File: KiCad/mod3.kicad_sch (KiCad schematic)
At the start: 49 parts, among them M5 Fan_4pin, M6 Fan_4pin, U3 ZD25Q64BSIGT

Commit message: Add most passive component footprints
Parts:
- C57, C58, C59, C60, C61, C62, C63, C64, C65, C66, C67, C68, C69, C70, C71, C72, C73, C74, C75, C76, C77, C78, C79: footprint Capacitor_SMD:C_0603_1608Metric -> Capacitor_SMD:C_0402_1005Metric
- D10, D9: footprint (none) -> LED_SMD:LED_0603_1608Metric
- D11, D12: footprint (none) -> Diode_SMD:D_SOD-123
- M5, M6: footprint (none) -> Connector:FanPinHeader_1x04_P2.54mm_Vertical
- R45, R57: value 510R -> 2.2k; footprint (none) -> Resistor_SMD:R_0402_1005Metric
- R46, R47, R48, R50, R51, R52, R53, R54, R56, R58, R61, R62: footprint (none) -> Resistor_SMD:R_0402_1005Metric
- R49: footprint (none) -> Resistor_SMD:R_0805_2012Metric
- R55, R59, R60: value 21.5k -> 22k; footprint (none) -> Resistor_SMD:R_0402_1005Metric
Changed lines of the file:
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@@
 			)
 		)
-		(property "Footprint" ""
+		(property "Footprint" "Resistor_SMD:R_0402_1005Metric"
 			(at 323.85 54.61 0)
 			(effects
@@
 			)
 		)
-		(property "Footprint" "Capacitor_SMD:C_0603_1608Metric"
+		(property "Footprint" "Capacitor_SMD:C_0402_1005Metric"
 			(at 223.52 168.91 0)
 			(effects
@@
 			)
 		)
-		(property "Footprint" "Capacitor_SMD:C_0603_1608Metric"
+		(property "Footprint" "Capacitor_SMD:C_0402_1005Metric"
 			(at 223.52 158.75 0)
 			(effects
@@
 			)
 		)
-		(property "Footprint" ""
+		(property "Footprint" "LED_SMD:LED_0603_1608Metric"
 			(at 320.04 153.67 0)
 			(effects
@@
 			)
 		)
-		(property "Footprint" ""
+		(property "Footprint" "Resistor_SMD:R_0402_1005Metric"
 			(at 320.04 128.27 0)
 			(effects
@@
 			)
 		)
-		(property "Value" "21.5k"
+		(property "Value" "22k"
 			(at 380.492 51.562 90)
 			(effects
@@
 			)
 		)
-		(property "Footprint" ""
+		(property "Footprint" "Resistor_SMD:R_0402_1005Metric"
 			(at 378.46 49.53 0)
 			(effects
@@
 			)
 		)
-		(property "Footprint" ""
+		(property "Footprint" "Connector:FanPinHeader_1x04_P2.54mm_Vertical"
 			(at 403.86 51.816 0)
 			(effects
@@
 			)
 		)
-		(property "Footprint" "Capacitor_SMD:C_0603_1608Metric"
+		(property "Footprint" "Capacitor_SMD:C_0402_1005Metric"
 			(at 223.52 163.83 0)
 			(effects
@@
 			)
 		)
-		(property "Footprint" ""
+		(property "Footprint" "Resistor_SMD:R_0402_1005Metric"
 			(at 321.31 250.19 0)
 			(effects
@@
 			)
 		)
-		(property "Footprint" ""
+		(property "Footprint" "Diode_SMD:D_SOD-123"
 			(at 382.27 44.45 0)
 			(effects
@@
 			)
 		)
-		(property "Footprint" "Capacitor_SMD:C_0603_1608Metric"
+		(property "Footprint" "Capacitor_SMD:C_0402_1005Metric"
 			(at 223.52 173.99 0)
 			(effects
@@
 			)
 		)
-		(property "Footprint" "Capacitor_SMD:C_0603_1608Metric"
+		(property "Footprint" "Capacitor_SMD:C_0402_1005Metric"
 			(at 320.04 44.45 0)
 			(effects
@@
 			)
 		)
-		(property "Value" "21.5k"
+		(property "Value" "22k"
 			(at 325.882 51.562 90)
 			(effects
@@
 			)
 		)
-		(property "Footprint" ""
+		(property "Footprint" "Resistor_SMD:R_0402_1005Metric"
 			(at 323.85 49.53 0)
 			(effects
@@
 			)
 		)
-		(property "Footprint" ""
+		(property "Footprint" "Resistor_SMD:R_0402_1005Metric"
 			(at 223.52 224.79 0)
 			(effects
@@
 			)
 		)
-		(property "Footprint" ""
+		(property "Footprint" "Resistor_SMD:R_0402_1005Metric"
 			(at 378.46 54.61 0)
 			(effects
@@
 			)
 		)
-		(property "Footprint" "Capacitor_SMD:C_0603_1608Metric"
+		(property "Footprint" "Capacitor_SMD:C_0402_1005Metric"
 			(at 223.52 140.97 0)
 			(effects
@@
 			)
 		)
-		(property "Footprint" "Capacitor_SMD:C_0603_1608Metric"
+		(property "Footprint" "Capacitor_SMD:C_0402_1005Metric"
 			(at 223.52 138.43 0)
 			(effects
@@
 			)
 		)
-		(property "Footprint" "Capacitor_SMD:C_0603_1608Metric"
+		(property "Footprint" "Capacitor_SMD:C_0402_1005Metric"
 			(at 223.52 115.57 0)
 			(effects
@@
 			)
 		)
-		(property "Footprint" "Capacitor_SMD:C_0603_1608Metric"
+		(property "Footprint" "Capacitor_SMD:C_0402_1005Metric"
 			(at 223.52 118.11 0)
 			(effects
@@
 			)
 		)
-		(property "Footprint" "Capacitor_SMD:C_0603_1608Metric"
+		(property "Footprint" "Capacitor_SMD:C_0402_1005Metric"
 			(at 223.52 107.95 0)
 			(effects
@@
 			)
 		)
-		(property "Footprint" "Capacitor_SMD:C_0603_1608Metric"
+		(property "Footprint" "Capacitor_SMD:C_0402_1005Metric"
 			(at 370.84 44.45 0)
 			(effects
@@
 			)
 		)
-		(property "Footprint" "Capacitor_SMD:C_0603_1608Metric"
+		(property "Footprint" "Capacitor_SMD:C_0402_1005Metric"
 			(at 223.52 95.25 0)
 			(effects
@@
 			)
 		)
-		(property "Footprint" ""
+		(property "Footprint" "Resistor_SMD:R_0402_1005Metric"
 			(at 223.52 300.99 0)
 			(effects
@@
 			)
 		)
-		(property "Footprint" "Capacitor_SMD:C_0603_1608Metric"
+		(property "Footprint" "Capacitor_SMD:C_0402_1005Metric"
 			(at 223.52 151.13 0)
 			(effects
@@
 			)
 		)
-		(property "Footprint" ""
+		(property "Footprint" "Resistor_SMD:R_0402_1005Metric"
 			(at 392.43 44.45 0)
 			(effects
@@
 			)
 		)
-		(property "Footprint" "Capacitor_SMD:C_0603_1608Metric"
+		(property "Footprint" "Capacitor_SMD:C_0402_1005Metric"
 			(at 223.52 171.45 0)
 			(effects
@@
 			)
 		)
-		(property "Footprint" "Capacitor_SMD:C_0603_1608Metric"
+		(property "Footprint" "Capacitor_SMD:C_0402_1005Metric"
 			(at 223.52 184.15 0)
 			(effects
@@
 			)
 		)
-		(property "Footprint" ""
+		(property "Footprint" "Resistor_SMD:R_0402_1005Metric"
 			(at 223.52 262.89 0)
 			(effects
@@
 			)
 		)
-		(property "Footprint" ""
+		(property "Footprint" "Diode_SMD:D_SOD-123"
 			(at 327.66 44.45 0)
 			(effects
@@
 			)
 		)
-		(property "Footprint" ""
+		(property "Footprint" "Resistor_SMD:R_0402_1005Metric"
 			(at 316.23 250.19 0)
 			(effects
@@
 			)
 		)
-		(property "Footprint" "Capacitor_SMD:C_0603_1608Metric"
+		(property "Footprint" "Capacitor_SMD:C_0402_1005Metric"
 			(at 223.52 161.29 0)
 			(effects
@@
 			)
 		)
-		(property "Footprint" "Capacitor_SMD:C_0603_1608Metric"
+		(property "Footprint" "Capacitor_SMD:C_0402_1005Metric"
 			(at 223.52 166.37 0)
 			(effects
@@
 			)
 		)
-		(property "Footprint" ""
+		(property "Footprint" "Resistor_SMD:R_0805_2012Metric"
 			(at 275.59 66.04 0)
 			(effects
@@
 			)
 		)
-		(property "Footprint" ""
+		(property "Footprint" "Connector:FanPinHeader_1x04_P2.54mm_Vertical"
 			(at 349.25 51.816 0)
 			(effects
@@
 			)
 		)
-		(property "Footprint" "Capacitor_SMD:C_0603_1608Metric"
+		(property "Footprint" "Capacitor_SMD:C_0402_1005Metric"
 			(at 223.52 105.41 0)
 			(effects
@@
 			)
 		)
-		(property "Footprint" "Capacitor_SMD:C_0603_1608Metric"
+		(property "Footprint" "Capacitor_SMD:C_0402_1005Metric"
 			(at 223.52 148.59 0)
 			(effects
@@
 			)
 		)
-		(property "Footprint" ""
+		(property "Footprint" "LED_SMD:LED_0603_1608Metric"
 			(at 209.55 77.47 0)
 			(effects
@@
 			)
 		)
-		(property "Footprint" ""
+		(property "Footprint" "Resistor_SMD:R_0402_1005Metric"
 			(at 316.23 276.86 0)
 			(effects
@@
 			)
 		)
-		(property "Footprint" "Capacitor_SMD:C_0603_1608Metric"
+		(property "Footprint" "Capacitor_SMD:C_0402_1005Metric"
 			(at 339.09 246.38 0)
 			(effects
@@
 			)
 		)
-		(property "Footprint" "Capacitor_SMD:C_0603_1608Metric"
+		(property "Footprint" "Capacitor_SMD:C_0402_1005Metric"
 			(at 223.52 176.53 0)
 			(effects
@@
 			)
 		)
-		(property "Footprint" ""
+		(property "Footprint" "Resistor_SMD:R_0402_1005Metric"
 			(at 337.82 44.45 0)
 			(effects
@@
 			)
 		)
-		(property "Footprint" ""
+		(property "Footprint" "Resistor_SMD:R_0402_1005Metric"
 			(at 320.04 125.73 0)
 			(effects
@@
 			)
 		)
-		(property "Value" "510R"
+		(property "Value" "2.2k"
 			(at 212.09 71.1199 0)
 			(effects
@@
 			)
 		)
-		(property "Footprint" ""
+		(property "Footprint" "Resistor_SMD:R_0402_1005Metric"
 			(at 209.55 69.85 0)
 			(effects
@@
 			)
 		)
-		(property "Value" "510R"
+		(property "Value" "2.2k"
 			(at 328.93 151.13 90)
 			(effects
@@
 			)
 		)
-		(property "Footprint" ""
+		(property "Footprint" "Resistor_SMD:R_0402_1005Metric"
 			(at 328.93 153.67 0)
 			(effects
@@
 			)
 		)
-		(property "Footprint" "Capacitor_SMD:C_0603_1608Metric"
+		(property "Footprint" "Capacitor_SMD:C_0402_1005Metric"
 			(at 223.52 97.79 0)
 			(effects
@@
 			)
 		)
-		(property "Footprint" "Capacitor_SMD:C_0603_1608Metric"
+		(property "Footprint" "Capacitor_SMD:C_0402_1005Metric"
 			(at 223.52 181.61 0)
 			(effects
@@
 			)
 		)
-		(property "Value" "21.5k"
+		(property "Value" "22k"
 			(at 377.19 60.9599 0)
 			(effects
@@
 			)
 		)
-		(property "Footprint" ""
+		(property "Footprint" "Resistor_SMD:R_0402_1005Metric"
 			(at 374.65 59.69 0)
 			(effects

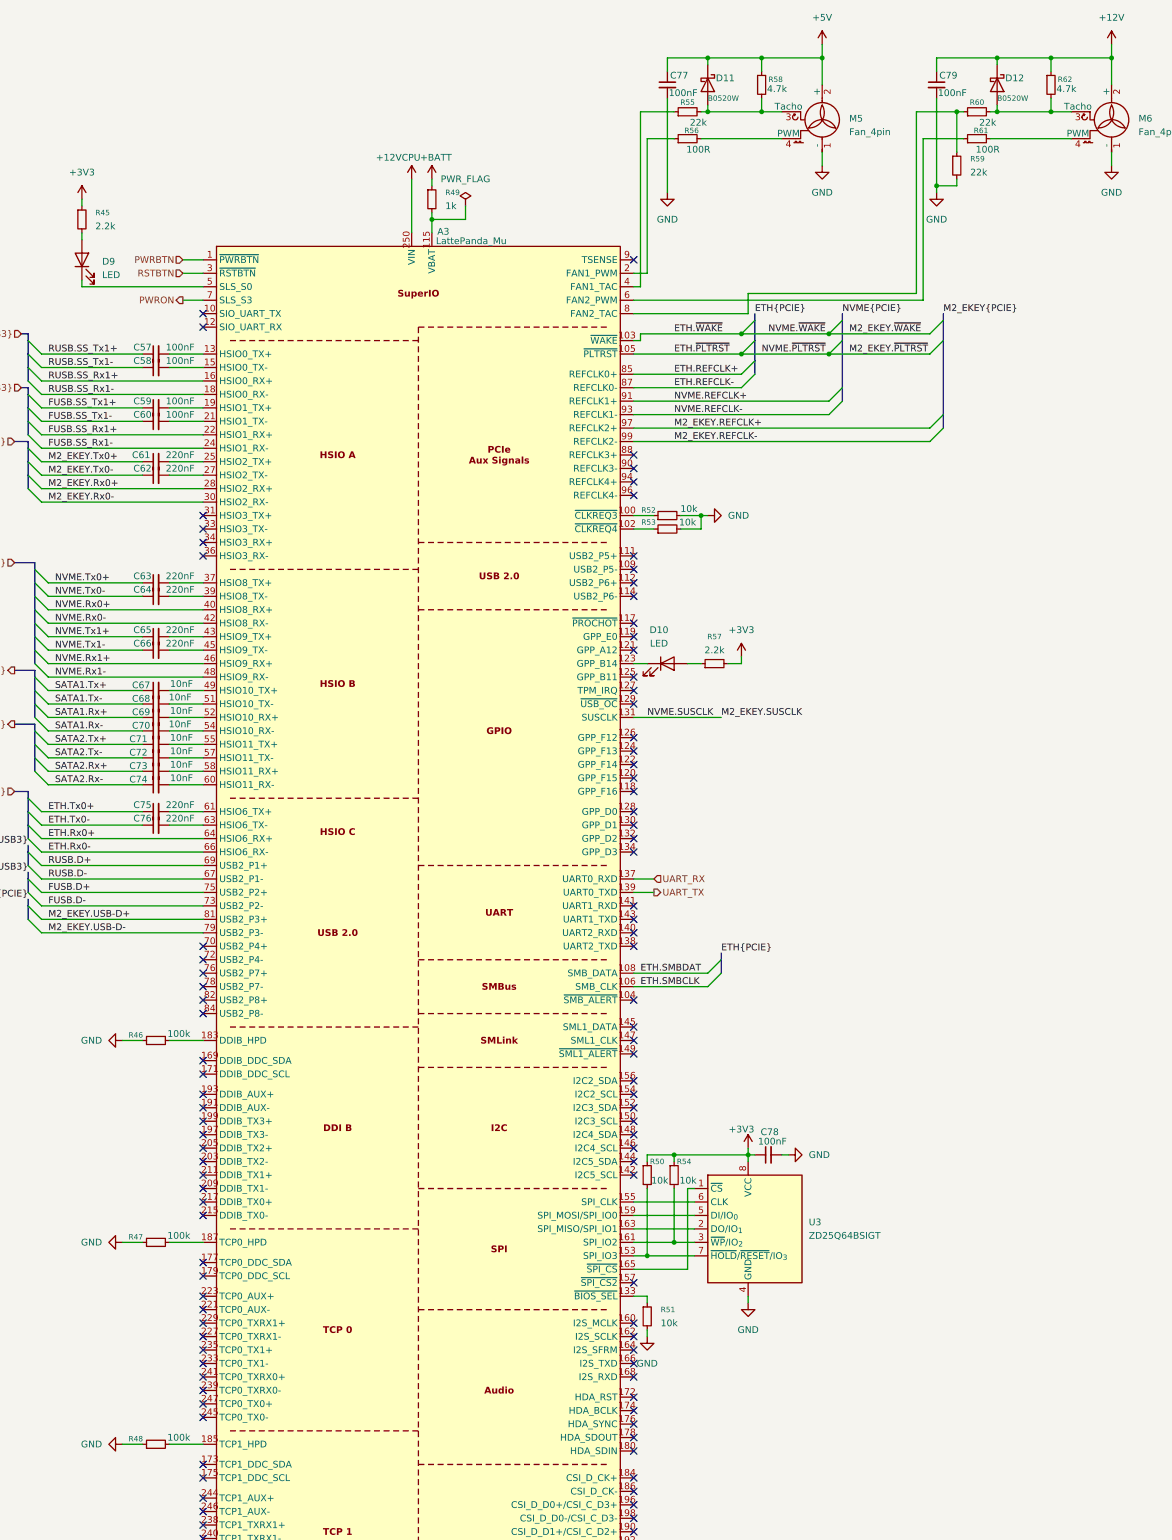
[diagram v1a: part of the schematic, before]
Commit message: Finish fixing footprints
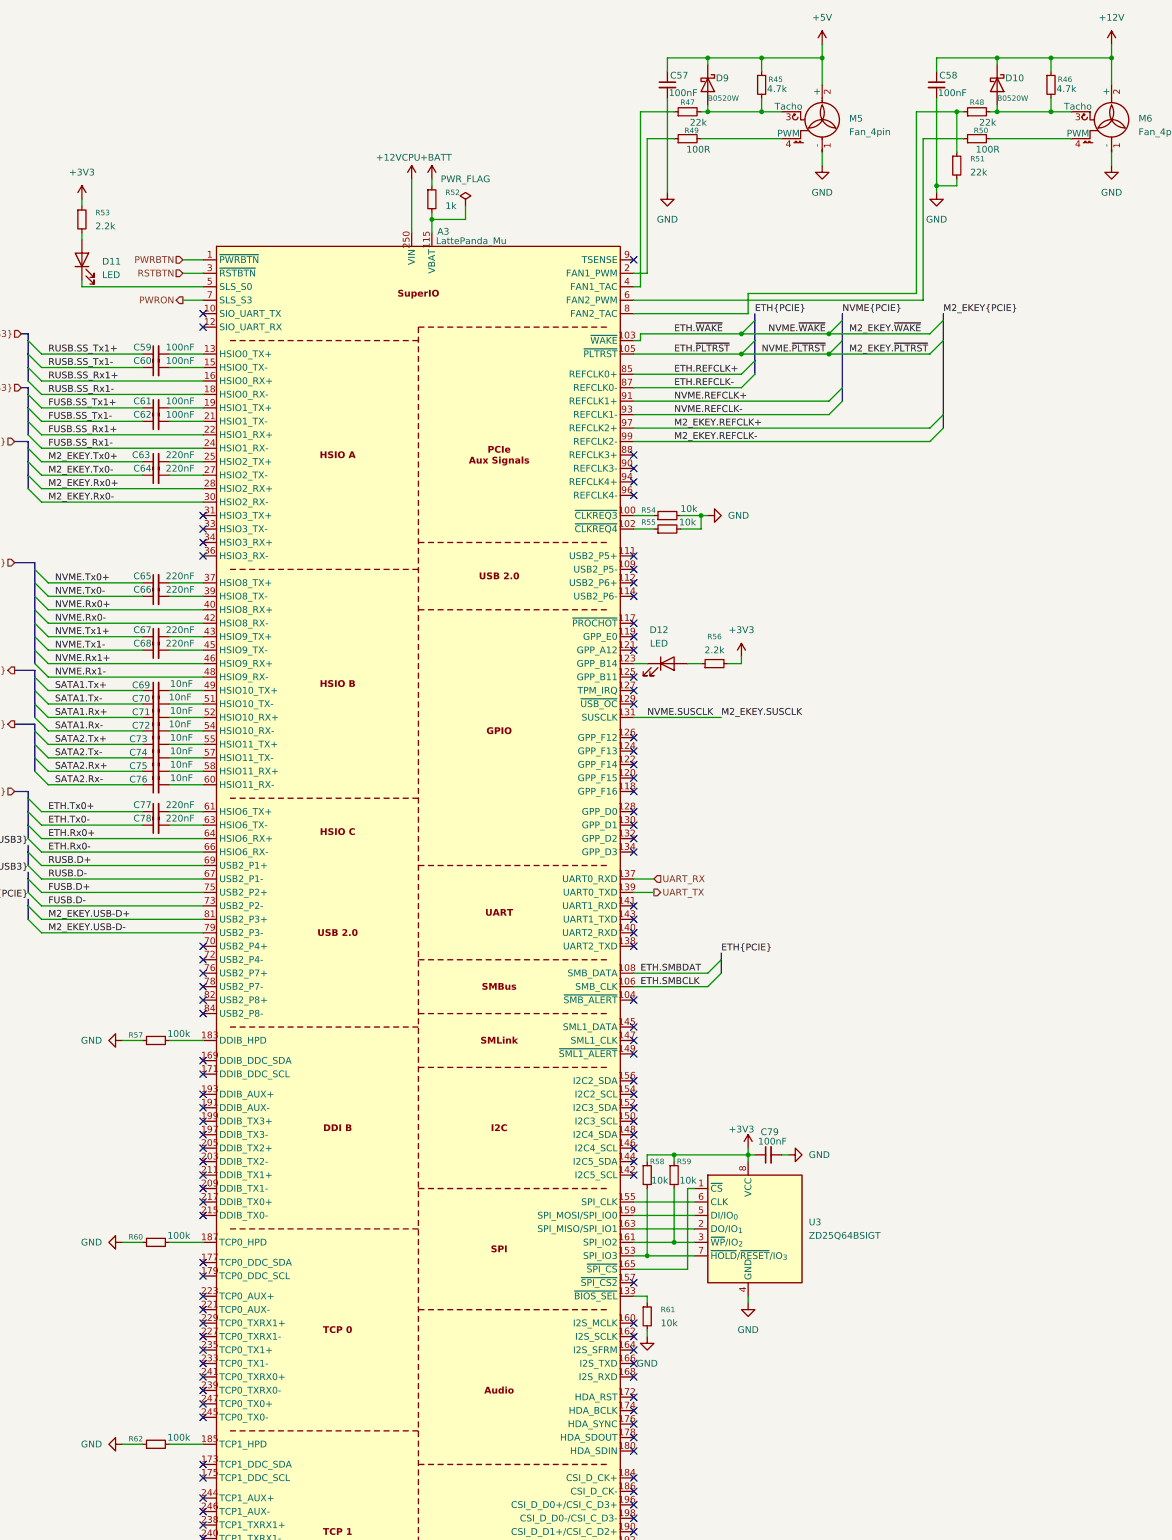
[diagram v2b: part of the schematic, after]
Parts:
- renumbered C77 to C57, C79 to C58, C57 to C59, C58 to C60, C59 to C61, C60 to C62, C61 to C63, C62 to C64, C63 to C65, C64 to C66, C65 to C67, C66 to C68, C67 to C69, C68 to C70, C69 to C71, C70 to C72, C71 to C73, C72 to C74, C73 to C75, C74 to C76, C75 to C77, C76 to C78, C78 to C79, D12 to D10, D9 to D11, D10 to D12, D11 to D9, R58 to R45, R62 to R46, R55 to R47, R60 to R48, R56 to R49, R61 to R50, R59 to R51, R49 to R52, R45 to R53, R52 to R54, R53 to R55, R57 to R56, R46 to R57, R50 to R58, R54 to R59, R47 to R60, R51 to R61, R48 to R62

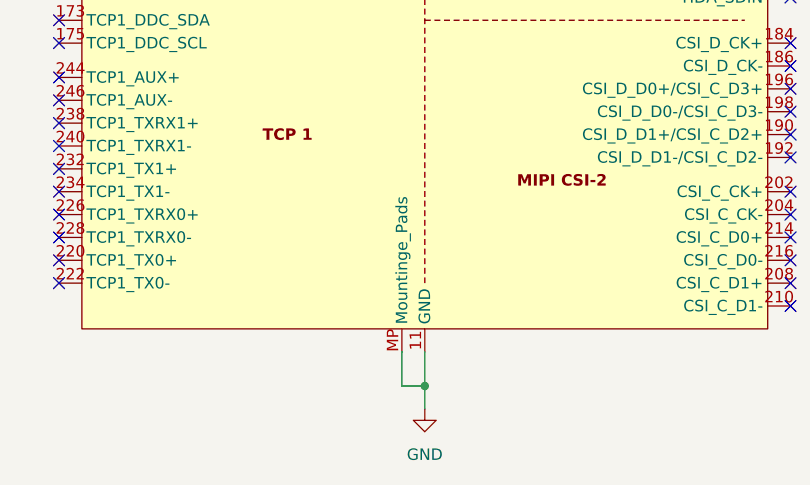
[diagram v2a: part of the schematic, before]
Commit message: Fix more footprint issues, continue laying out components
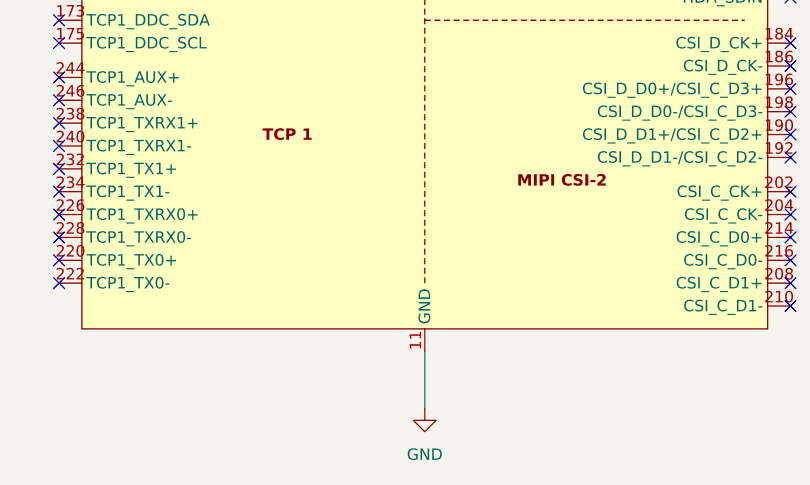
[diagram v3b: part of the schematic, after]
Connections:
- net GND: no longer A3.MP (Mountinge_Pads)
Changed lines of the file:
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@@
 	)
 	(junction
-		(at 273.05 345.44)
-		(diameter 0)
-		(color 0 0 0 0)
-	)
-	(junction
 		(at 392.43 39.37)
 		(diameter 0)
@@
 	(wire
 		(pts
-			(xy 273.05 341.63) (xy 273.05 345.44)
-		)
-		(stroke
-			(width 0)
-			(type default)
-		)
-	)
-	(wire
-		(pts
 			(xy 350.52 91.44) (xy 369.57 91.44)
 		)
@@
 	(wire
 		(pts
-			(xy 270.51 345.44) (xy 273.05 345.44)
-		)
-		(stroke
-			(width 0)
-			(type default)
-		)
-	)
-	(wire
-		(pts
 			(xy 203.2 146.05) (xy 232.41 146.05)
 		)
@@
 	(wire
 		(pts
-			(xy 270.51 341.63) (xy 270.51 345.44)
-		)
-		(stroke
-			(width 0)
-			(type default)
-		)
-	)
-	(wire
-		(pts
 			(xy 321.31 246.38) (xy 335.28 246.38)
 		)
@@
 	(wire
 		(pts
-			(xy 273.05 345.44) (xy 273.05 347.98)
+			(xy 273.05 341.63) (xy 273.05 347.98)
 		)
 		(stroke
@@
 		(pin "93"
 		)
-		(pin "MP"
-		)
 		(pin "184"

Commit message: Place STM32 and fix cpu fan headers
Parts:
- M5: footprint Connector:FanPinHeader_1x04_P2.54mm_Vertical -> Connector_JST:JST_PH_B4B-PH-K_1x04_P2.00mm_Vertical
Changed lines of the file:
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@@
 			)
 		)
-		(property "Footprint" "Connector:FanPinHeader_1x04_P2.54mm_Vertical"
+		(property "Footprint" "Connector_JST:JST_PH_B4B-PH-K_1x04_P2.00mm_Vertical"
 			(at 349.25 51.816 0)
 			(effects
